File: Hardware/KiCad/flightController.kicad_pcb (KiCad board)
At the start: 4 copper layers, 57 x 57 mm, 183 parts, among them J1 USB_B_Mini, J10 JST SH1-2P, J11 MOLEX 5268-7P, J12 JST SH1-8P, J2 USB_B_Mini, J3 2.54mm header, J4 2.54mm header, J5 TF-01A, J6 1mm header, J7 JST SH1-4P, J8 JST SH1-4P, J9 JST SH1-4P, Q1 PMBT3904, Q2 PMBT3904, SW1 SW_SPDT, SW2 SW_Push, U1 MPU-6000, U10 CH330N, U11 SMF05CT1G, U12 SMF05CT1G, U13 SMF05CT1G, U2 HMC5883L, U3 FM24C64B, U4 BMP388, U5 STM32H743VIT6, U6 AMS1117-5V, U7 SPX3819M5-L-3-3/TR, U8 SMF05CT1G, U9 SMF05CT1G

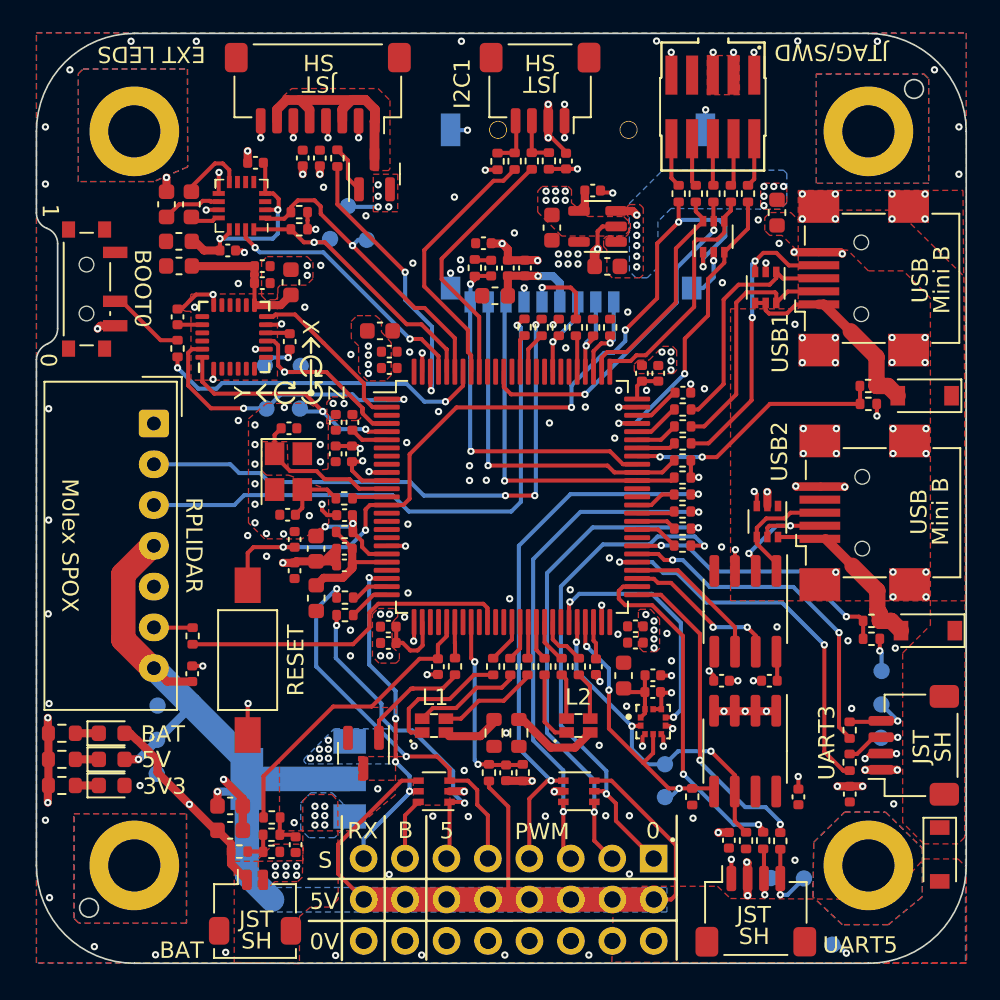
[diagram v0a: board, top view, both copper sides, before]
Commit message: Finalizing V1.0 PCB, design send off for production
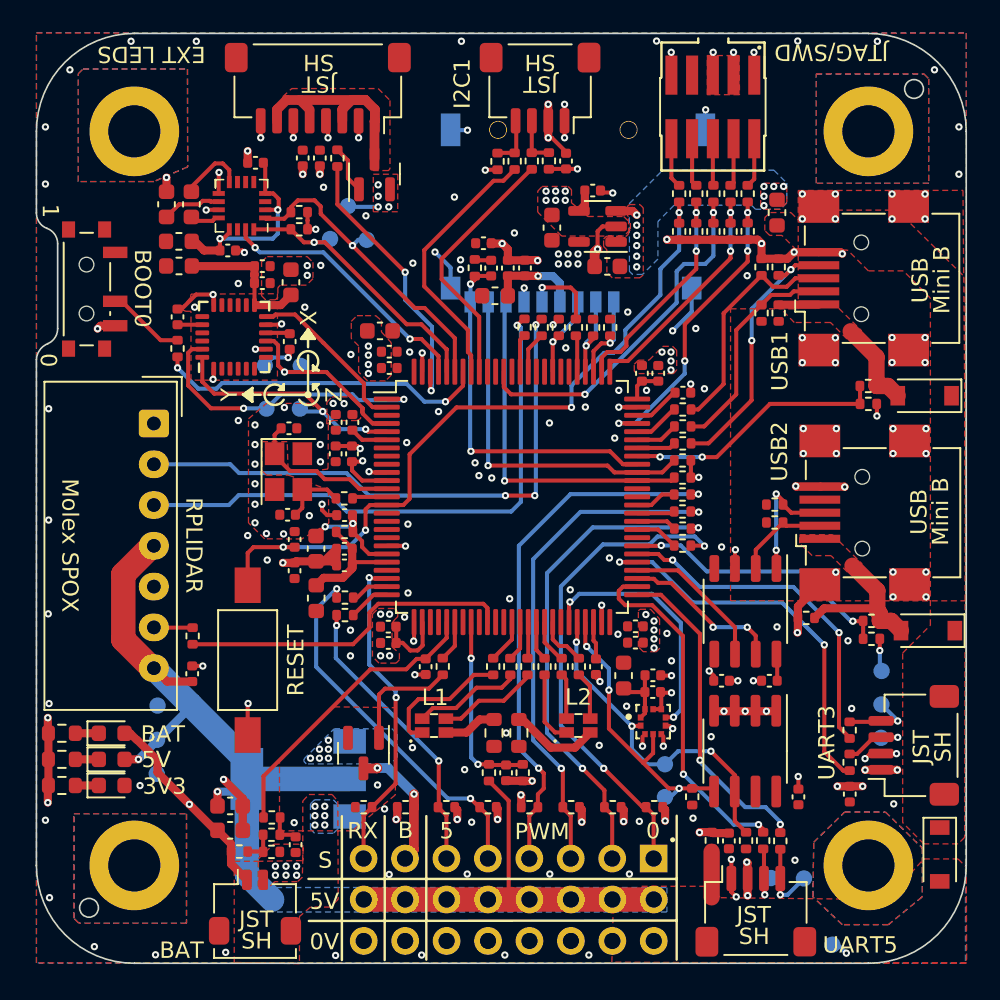
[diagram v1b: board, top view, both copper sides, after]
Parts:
- removed U11, U12, U13, U8, U9: SMF05CT1G, Package_TO_SOT_SMD:SOT-363_SC-70-6
- added D10: LXES15AAA1-133, Resistor_SMD:R_0402_1005Metric, F.Cu at (114.5, 91.3)
- added D11: LXES15AAA1-133, Resistor_SMD:R_0402_1005Metric, F.Cu at (114.5, 94.2)
- added D12: LXES15AAA1-133, Resistor_SMD:R_0402_1005Metric, F.Cu at (115.5, 91.3)
- added D13: LXES15AAA1-133, Resistor_SMD:R_0402_1005Metric, F.Cu at (117.2, 112.8)
- added D14: LXES15AAA1-133, Resistor_SMD:R_0402_1005Metric, F.Cu at (115.3, 105.9)
- added D15: LXES15AAA1-133, Resistor_SMD:R_0402_1005Metric, F.Cu at (115.3, 107.0)
- added D16: LXES15AAA1-133, Resistor_SMD:R_0402_1005Metric, F.Cu at (113.6, 89.2)
- added D17: LXES15AAA1-133, Resistor_SMD:R_0402_1005Metric, F.Cu at (112.5, 89.2)
- added D18: LXES15AAA1-133, Resistor_SMD:R_0402_1005Metric, F.Cu at (107.9, 124.5)
- added D19: LXES15AAA1-133, Resistor_SMD:R_0402_1005Metric, F.Cu at (111.5, 89.2)
- added D20: LXES15AAA1-133, Resistor_SMD:R_0402_1005Metric, F.Cu at (105.3, 124.5)
- added D21: LXES15AAA1-133, Resistor_SMD:R_0402_1005Metric, F.Cu at (110.5, 89.2)
- added D22: LXES15AAA1-133, Resistor_SMD:R_0402_1005Metric, F.Cu at (102.8, 124.5)
- added D23: LXES15AAA1-133, Resistor_SMD:R_0402_1005Metric, F.Cu at (109.4, 89.2)
- added D24: LXES15AAA1-133, Resistor_SMD:R_0402_1005Metric, F.Cu at (100.2, 124.5)
- added D25: LXES15AAA1-133, Resistor_SMD:R_0402_1005Metric, F.Cu at (97.7, 124.5)
- added D26: LXES15AAA1-133, Resistor_SMD:R_0402_1005Metric, F.Cu at (95.1, 124.5)
- added D27: LXES15AAA1-133, Resistor_SMD:R_0402_1005Metric, F.Cu at (92.6, 124.5)
- added D28: LXES15AAA1-133, Resistor_SMD:R_0402_1005Metric, F.Cu at (90.1, 124.5)
- added D29: LXES15AAA1-133, Resistor_SMD:R_0402_1005Metric, F.Cu at (111.4, 126.5)
- added D9: LXES15AAA1-133, Resistor_SMD:R_0402_1005Metric, F.Cu at (115.5, 94.2)
- U10: footprint Package_SO:SOIC-8_3.9x4.9mm_P1.27mm -> Package_SO:SOP-8_3.9x4.9mm_P1.27mm
- moved C14 0.75 mm to (93.9, 115.8)
- moved R16 0.75 mm to (94.9, 115.8)
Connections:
- C41 pad 1: Net-(C41-Pad1) -> +3V3
- U10 pad 8: Net-(C41-Pad1) -> +3V3
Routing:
- net +5V: track 90.0 -> 70.2 mm
- net GND: track 98.2 -> 115.9 mm, vias 167 -> 173
- net NRST: track 51.2 -> 44.9 mm, vias 6 -> 4
- net Net-(D7-Pad2): track 13.0 -> 8.00 mm
- net BUZZ_IN: track 3.82 -> 7.95 mm, vias 0 -> 2
- net Net-(D12-Pad2): track 18.6 -> 16.5 mm
- net PWM5: track 19.8 -> 17.7 mm
- net +3V3: track 32.2 -> 34.2 mm, vias 109 -> 107
- net USB_DM: track 15.5 -> 13.6 mm
- net Net-(C41-Pad1): track 1.73 -> 0.00 mm
- net Net-(J2-Pad2): track 7.67 -> 6.00 mm, vias 2 -> 0
- net SWO/TDO: track 21.0 -> 22.6 mm
- net PWM3: track 34.2 -> 33.0 mm
- net UART4_RX: track 21.1 -> 19.8 mm, vias 4 -> 2
- net Net-(J2-Pad3): track 6.96 -> 7.99 mm, vias 0 -> 2
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- added copper zone on F.Cu, net Net-(D7-Pad2)
- added copper zone on F.Cu, net Net-(D8-Pad2)
- removed copper zone on F.Cu, net BUZZ_IN
